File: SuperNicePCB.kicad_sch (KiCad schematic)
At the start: 0 parts

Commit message: Add subsection
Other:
- added sheet HumanSesors (HumanSensors.kicad_sch)
- added sheet MCU (MCU.kicad_sch)
- added sheet Power (Power.kicad_sch)
- added sheet UWB (UWB.kicad_sch)
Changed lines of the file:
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@@
 	(generator_version "10.0")
 	(paper "A4")
+	(sheet
+		(at 49.53 30.48)
+		(size 83.82 60.96)
+		(exclude_from_sim no)
+		(in_bom yes)
+		(on_board yes)
+		(dnp no)
+		(fields_autoplaced yes)
+		(stroke
+			(width 0.1524)
+			(type solid)
+		)
+		(fill
+			(color 0 0 0 0)
+		)
+		(property "Sheetname" "MCU"
+			(at 49.53 29.7684 0)
+			(show_name no)
+			(do_not_autoplace no)
+			(effects
+				(font
+					(size 1.27 1.27)
+				)
+				(justify left bottom)
+			)
+		)
+		(property "Sheetfile" "MCU.kicad_sch"
+			(at 49.53 92.0246 0)
+			(show_name no)
+			(do_not_autoplace no)
+			(effects
+				(font
+					(size 1.27 1.27)
+				)
+				(justify left top)
+			)
+		)
+		(instances
+			(project "SuperNicePCB"
+				(path "/794e52b0-48ac-4476-a221-597be743d898"
+					(page "2")
+				)
+			)
+		)
+	)
+	(sheet
+		(at 156.21 101.6)
+		(size 83.82 62.23)
+		(exclude_from_sim no)
+		(in_bom yes)
+		(on_board yes)
+		(dnp no)
+		(fields_autoplaced yes)
+		(stroke
+			(width 0.1524)
+			(type solid)
+		)
+		(fill
+			(color 0 0 0 0)
+		)
+		(property "Sheetname" "HumanSesors"
+			(at 156.21 100.8884 0)
+			(show_name no)
+			(do_not_autoplace no)
+			(effects
+				(font
+					(size 1.27 1.27)
+				)
+				(justify left bottom)
+			)
+		)
+		(property "Sheetfile" "HumanSensors.kicad_sch"
+			(at 156.21 164.4146 0)
+			(show_name no)
+			(do_not_autoplace no)
+			(effects
+				(font
+					(size 1.27 1.27)
+				)
+				(justify left top)
+			)
+		)
+		(instances
+			(project "SuperNicePCB"
+				(path "/794e52b0-48ac-4476-a221-597be743d898"
+					(page "4")
+				)
+			)
+		)
+	)
+	(sheet
+		(at 156.21 30.48)
+		(size 85.09 59.69)
+		(exclude_from_sim no)
+		(in_bom yes)
+		(on_board yes)
+		(dnp no)
+		(fields_autoplaced yes)
+		(stroke
+			(width 0.1524)
+			(type solid)
+		)
+		(fill
+			(color 0 0 0 0)
+		)
+		(property "Sheetname" "Power"
+			(at 156.21 29.7684 0)
+			(show_name no)
+			(do_not_autoplace no)
+			(effects
+				(font
+					(size 1.27 1.27)
+				)
+				(justify left bottom)
+			)
+		)
+		(property "Sheetfile" "Power.kicad_sch"
+			(at 156.21 90.7546 0)
+			(show_name no)
+			(do_not_autoplace no)
+			(effects
+				(font
+					(size 1.27 1.27)
+				)
+				(justify left top)
+			)
+		)
+		(instances
+			(project "SuperNicePCB"
+				(path "/794e52b0-48ac-4476-a221-597be743d898"
+					(page "3")
+				)
+			)
+		)
+	)
+	(sheet
+		(at 49.53 100.33)
+		(size 83.82 60.96)
+		(exclude_from_sim no)
+		(in_bom yes)
+		(on_board yes)
+		(dnp no)
+		(fields_autoplaced yes)
+		(stroke
+			(width 0.1524)
+			(type solid)
+		)
+		(fill
+			(color 0 0 0 0)
+		)
+		(property "Sheetname" "UWB"
+			(at 49.53 99.6184 0)
+			(show_name no)
+			(do_not_autoplace no)
+			(effects
+				(font
+					(size 1.27 1.27)
+				)
+				(justify left bottom)
+			)
+		)
+		(property "Sheetfile" "UWB.kicad_sch"
+			(at 49.53 161.8746 0)
+			(show_name no)
+			(do_not_autoplace no)
+			(effects
+				(font
+					(size 1.27 1.27)
+				)
+				(justify left top)
+			)
+		)
+		(instances
+			(project "SuperNicePCB"
+				(path "/794e52b0-48ac-4476-a221-597be743d898"
+					(page "5")
+				)
+			)
+		)
+	)
 	(sheet_instances
 		(path "/"

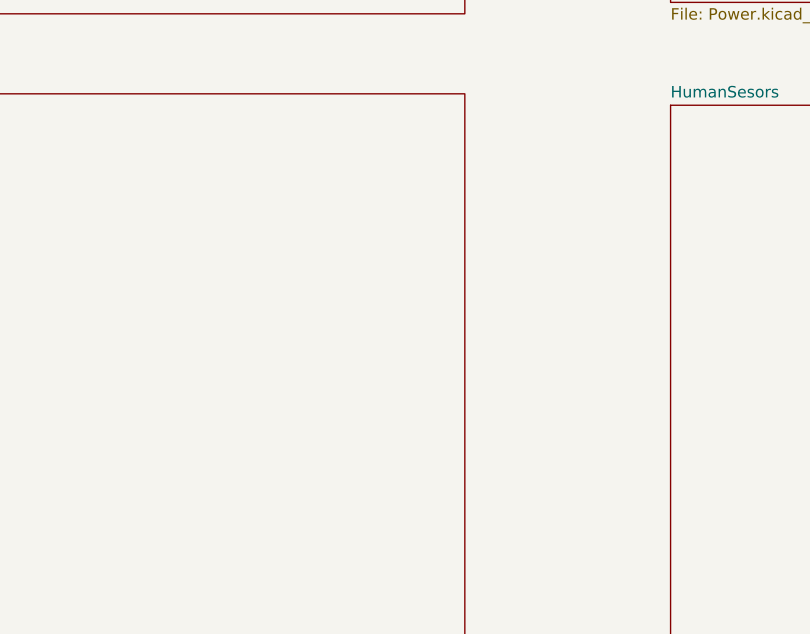
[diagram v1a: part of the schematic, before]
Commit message: Clean: deduplicate symbol library and fix UUIDs
- libs/lcsc/symbols/lcsc_imported.kicad_sym: merged 4 concatenated
  kicad_symbol_lib sections into one. Removed 8 duplicate symbol
  definitions (SCD40-D-R1, SHT40-AD1B-R3, DWM3000TR13, 0603,
  CC0603MRX5R5BB226, 22pF_(220), ESP32-S3-WROOM-1-N8 and their _1_1
  sub-units). Library reduced from 6407 to 4416 lines.
- mcu.kicad_sch: fix duplicate UUIDs on decoupling cap pins
- SuperNicePCB.kicad_sch: add missing UWB hierarchical label pins
  (UWB_CLK, UWB_CSn, UWB_IRQ, UWB_MISO, UWB_MOSI, UWB_RSTn, UWB_WAKE)
- SuperNicePCB.kicad_pro: clear stale used_designators cache
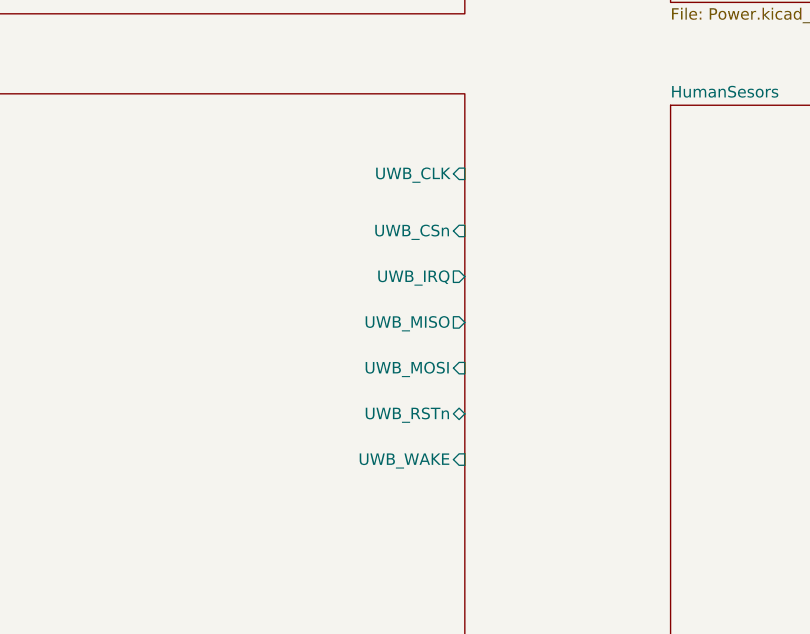
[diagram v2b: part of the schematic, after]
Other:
- sheet UWB ports: added UWB_CLK, UWB_CSn, UWB_IRQ, UWB_MISO, UWB_MOSI, UWB_RSTn, UWB_WAKE; removed none
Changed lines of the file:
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@@
+			)
+		)
+		(pin "UWB_CLK" input
+			(at 133.35 109.22 0)
+			(effects
+				(font
+					(size 1.27 1.27)
+				)
+				(justify right)
+			)
+		)
+		(pin "UWB_CSn" input
+			(at 133.35 115.57 0)
+			(effects
+				(font
+					(size 1.27 1.27)
+				)
+				(justify right)
+			)
+		)
+		(pin "UWB_IRQ" output
+			(at 133.35 120.65 0)
+			(effects
+				(font
+					(size 1.27 1.27)
+				)
+				(justify right)
+			)
+		)
+		(pin "UWB_MISO" output
+			(at 133.35 125.73 0)
+			(effects
+				(font
+					(size 1.27 1.27)
+				)
+				(justify right)
+			)
+		)
+		(pin "UWB_MOSI" input
+			(at 133.35 130.81 0)
+			(effects
+				(font
+					(size 1.27 1.27)
+				)
+				(justify right)
+			)
+		)
+		(pin "UWB_RSTn" bidirectional
+			(at 133.35 135.89 0)
+			(effects
+				(font
+					(size 1.27 1.27)
+				)
+				(justify right)
+			)
+		)
+		(pin "UWB_WAKE" input
+			(at 133.35 140.97 0)
+			(effects
+				(font
+					(size 1.27 1.27)
+				)
+				(justify right)
 			)
 		)

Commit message: Final Routing
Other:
- sheet HumanSesors ports: added 3.3V, AC_BCLK, AC_LRCLK, CO2_SCL, CO2_SDA, D_IN, PIR_OUT, R_RX0, R_TXO, Temp_SCL, Temp_SDA, U0_CTS, U0_RTS; removed none
- sheet MCU ports: added AC_BCLK, AC_DIN, AC_DOUT, AC_LRCLK, CO2_SCL, CO2_SDA, PIR_OUT, TEMP_SCL, TEMP_SDA, U0_CTS, U0_RTS, U0_RXD, U0_TXD, USB_D+, USB_D-, UWB_CS0, UWB_IRQ, UWB_MISO, UWB_MOSI, UWB_RST, UWB_RXOK, UWB_SCK, UWB_WAKEUP, VDD; removed none
- sheet Power ports: added +3.3V_Main, +3.3V_Sensors, USB_Data+, USB_Data-; removed none
- sheet UWB ports: added +3.3V_Sensors, UWB_RXOK; removed none

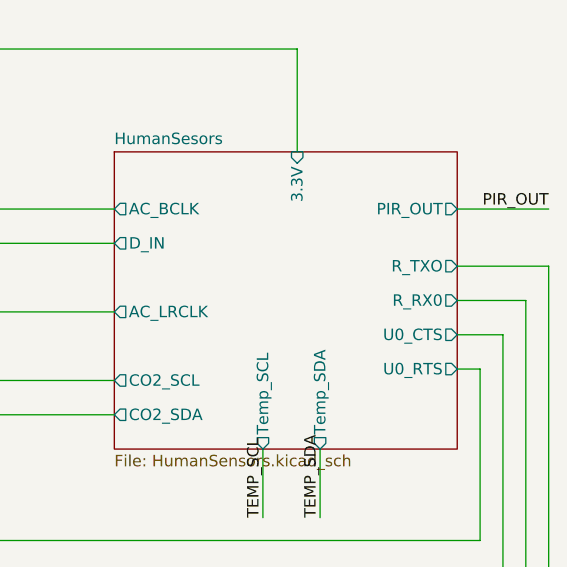
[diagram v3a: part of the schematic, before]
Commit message: KiCad: PCB placement, routing and schematic updates
Wiring of component blocks and sensors + component rearrangement + routing
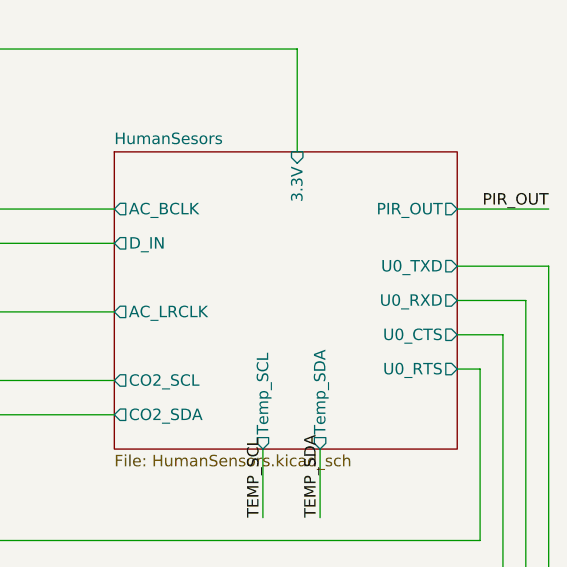
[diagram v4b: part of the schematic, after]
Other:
- sheet HumanSesors ports: added U0_RXD, U0_TXD; removed R_RX0, R_TXO
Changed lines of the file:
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@@
 			)
 		)
-		(pin "R_RX0" output
+		(pin "U0_RXD" output
 			(at 245.11 87.63 0)
 			(effects
@@
 			)
 		)
-		(pin "R_TXO" output
+		(pin "U0_TXD" output
 			(at 245.11 83.82 0)
 			(effects

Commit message: Finish data lines
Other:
- sheet UWB ports: added UWB_CS0, UWB_RST, UWB_SCK, UWB_WAKEUP; removed UWB_CLK, UWB_CSn, UWB_RSTn, UWB_WAKE
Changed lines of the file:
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@@
 			)
 		)
-		(pin "UWB_CLK" input
-			(at 72.39 76.2 0)
+		(pin "+3.3V_Sensors" input
+			(at 57.15 72.39 90)
 			(effects
 				(font
@@
 			)
 		)
-		(pin "UWB_CSn" input
+		(pin "UWB_CS0" output
 			(at 72.39 80.01 0)
 			(effects
@@
 			)
 		)
-		(pin "UWB_MOSI" input
+		(pin "UWB_MOSI" output
 			(at 72.39 91.44 0)
 			(effects
@@
 			)
 		)
-		(pin "UWB_RSTn" bidirectional
+		(pin "UWB_RST" output
 			(at 72.39 102.87 0)
 			(effects
@@
 			)
 		)
-		(pin "UWB_WAKE" input
-			(at 72.39 99.06 0)
-			(effects
-				(font
-					(size 1.27 1.27)
-				)
-				(justify right)
-			)
-		)
-		(pin "UWB_RXOK" input
+		(pin "UWB_RXOK" output
 			(at 72.39 95.25 0)
 			(effects
@@
 			)
 		)
-		(pin "+3.3V_Sensors" input
-			(at 57.15 72.39 90)
+		(pin "UWB_SCK" output
+			(at 72.39 76.2 0)
 			(effects
 				(font
+					(size 1.27 1.27)
+				)
+				(justify right)
+			)
+		)
+		(pin "UWB_WAKEUP" output
+			(at 72.39 99.06 0)
+			(effects
+				(font

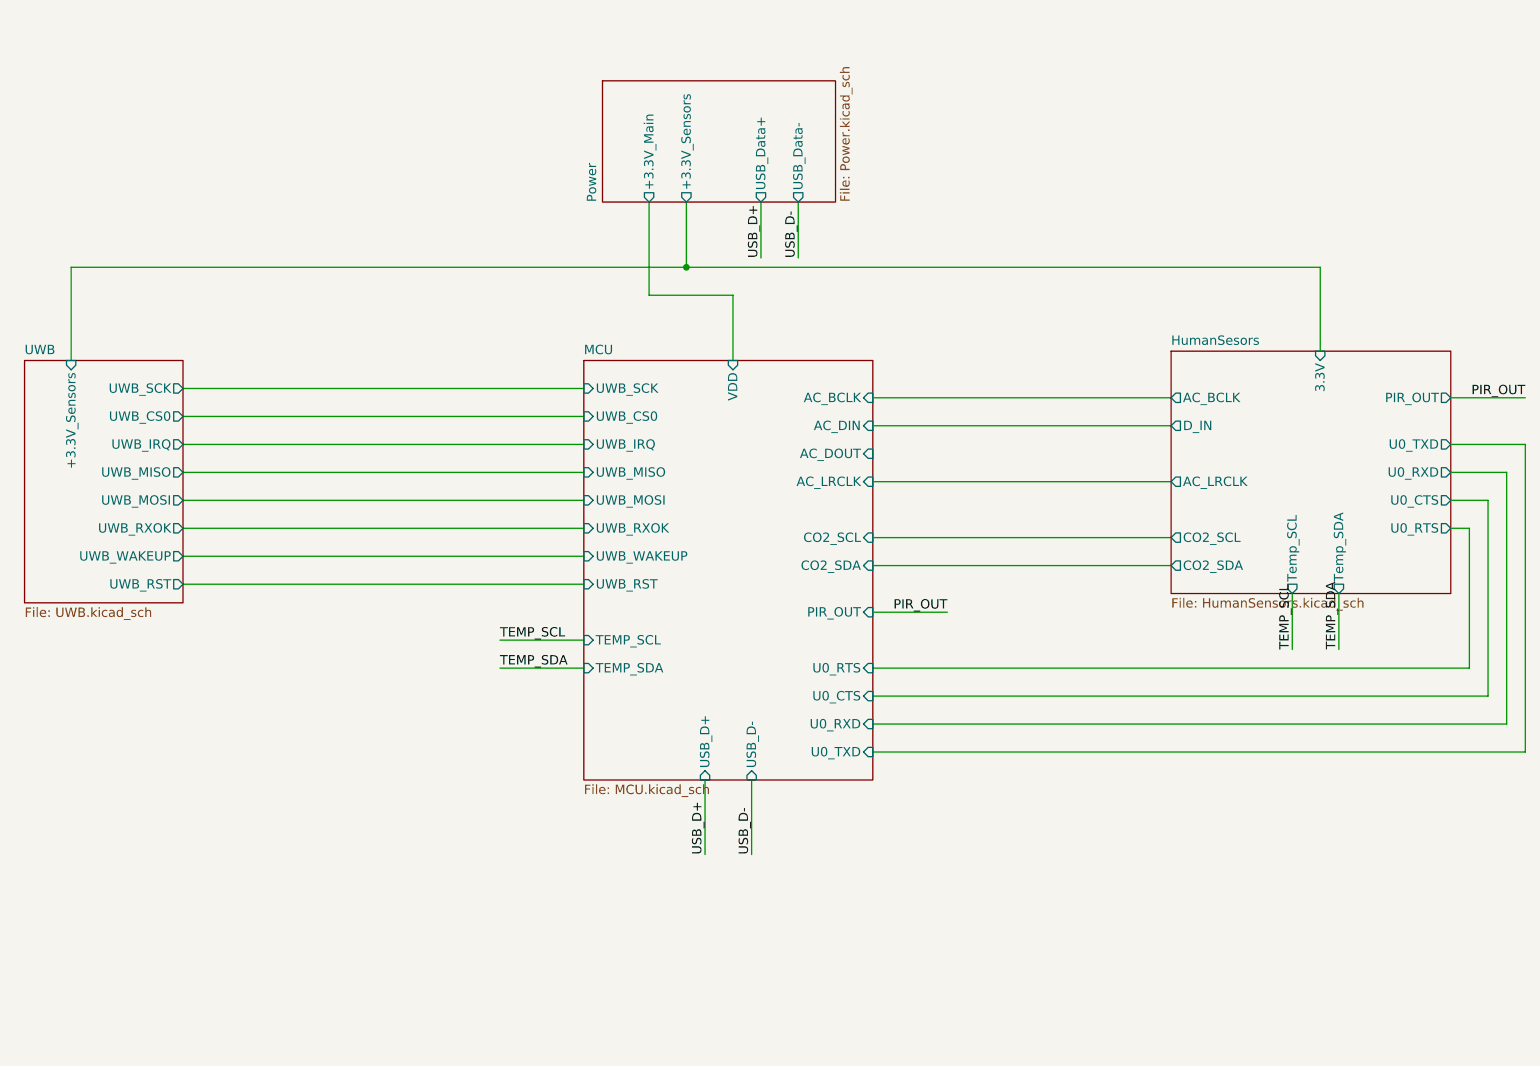
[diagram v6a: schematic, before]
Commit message: Rerouting
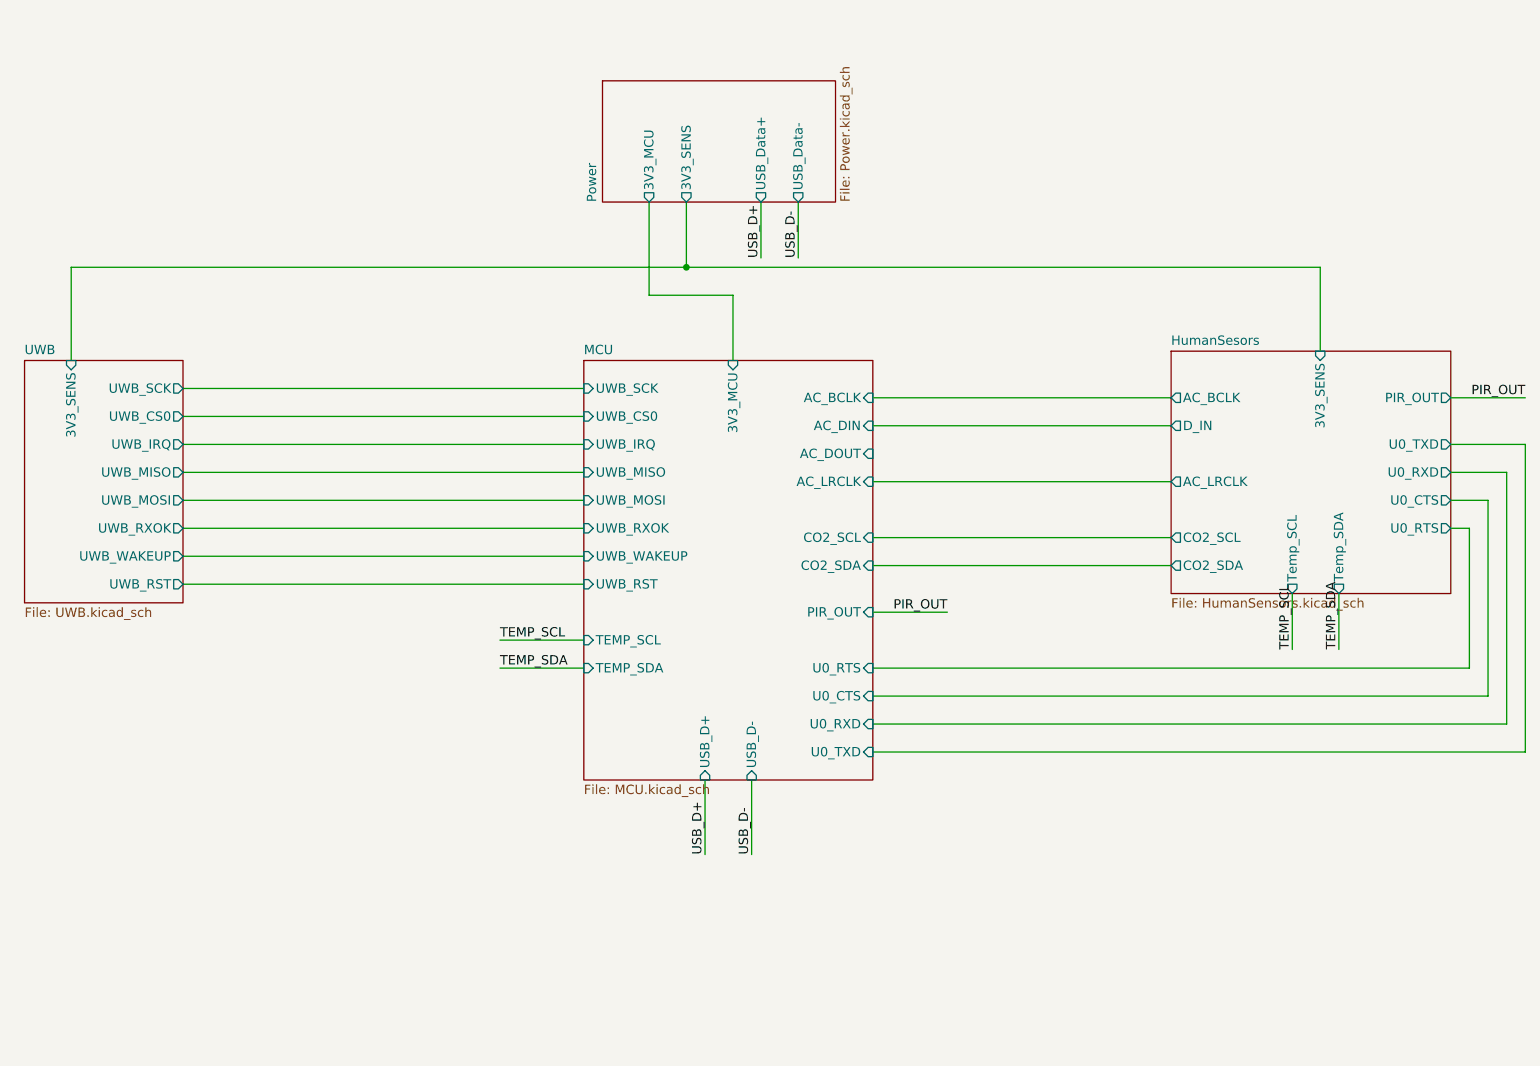
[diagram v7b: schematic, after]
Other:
- sheet HumanSesors ports: added 3V3_SENS; removed 3.3V
- sheet MCU ports: added 3V3_MCU; removed VDD
- sheet Power ports: added 3V3_MCU, 3V3_SENS; removed +3.3V_Main, +3.3V_Sensors
- sheet UWB ports: added 3V3_SENS; removed +3.3V_Sensors
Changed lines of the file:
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@@
 			)
 		)
-		(pin "VDD" input
+		(pin "3V3_MCU" input
 			(at 147.32 72.39 90)
 			(effects
@@
 			)
 		)
-		(pin "3.3V" input
+		(pin "3V3_SENS" input
 			(at 227.33 71.12 90)
 			(effects
@@
 			)
 		)
-		(pin "+3.3V_Main" output
+		(pin "3V3_MCU" output
 			(at 135.89 50.8 270)
 			(effects
@@
 			)
 		)
-		(pin "+3.3V_Sensors" output
+		(pin "3V3_SENS" output
 			(at 140.97 50.8 270)
 			(effects
@@
 			)
 		)
-		(pin "+3.3V_Sensors" input
+		(pin "3V3_SENS" input
 			(at 57.15 72.39 90)
 			(effects
